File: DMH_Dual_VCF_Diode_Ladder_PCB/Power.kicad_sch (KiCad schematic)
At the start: 32 parts, among them J0 Conn_01x01, J100 IDC_02x08, U1 TL074, U2 TL074, U3 TL074, U4 TL074, U5 TL074, U6 TL074, U7 TL074

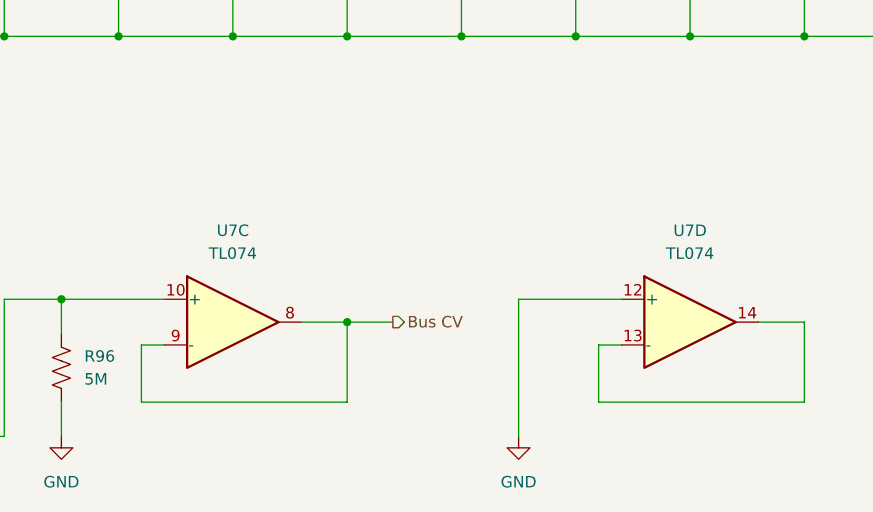
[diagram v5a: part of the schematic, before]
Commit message: Re-annotated OpAmps as per PCB layout
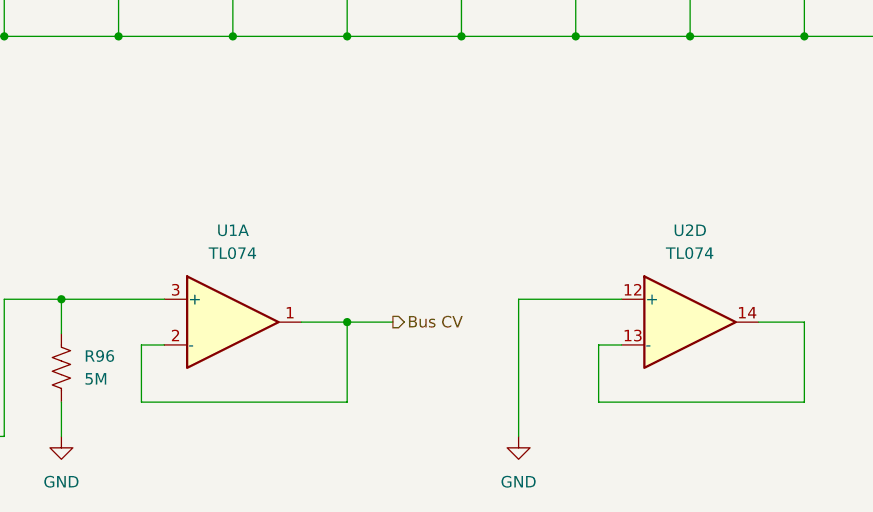
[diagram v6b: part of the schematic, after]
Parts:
- renumbered U7 to U1, U7 to U2
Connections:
- net Bus CV: now also U1.1, U1.2 (-); no longer U1.8, U1.9 (-)
- net at J100.7a (Pin_7a), J100.7b (Pin_7b), R96.1: now also U1.3 (+); no longer U1.10 (+)
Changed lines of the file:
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@@
+			)
+		)
+		(property "Function" ""
+			(at 167.64 120.65 0)
+			(effects
+				(font
+					(size 1.27 1.27)
+				)
 			)
 		)
@@
 		(dnp no)
 		(fields_autoplaced yes)
-		(property "Reference" "U7"
+		(property "Reference" "U2"
 			(at 152.4 167.64 0)
 			(effects
@@
 			)
 		)
+		(property "Function" ""
+			(at 152.4 177.8 0)
+			(effects
+				(font
+					(size 1.27 1.27)
+				)
+			)
+		)
 		(pin "10"
 		)
@@
 			(project ""
 				(path "/58f4306d-5387-4983-bb08-41a2313fd315/0cdf34b2-39cd-4d9e-981a-97cd34791509"
-					(reference "U7")
+					(reference "U2")
 					(unit 4)
 				)
@@
 			)
 		)
+		(property "Function" ""
+			(at 142.24 120.65 0)
+			(effects
+				(font
+					(size 1.27 1.27)
+				)
+			)
+		)
 		(pin "7"
 		)
@@
 			)
 		)
+		(property "Function" ""
+			(at 218.44 120.65 0)
+			(effects
+				(font
+					(size 1.27 1.27)
+				)
+			)
+		)
 		(pin "3"
 		)
@@
 				)
 				(hide yes)
+			)
+		)
+		(property "Function" ""
+			(at 116.84 120.65 0)
+			(effects
+				(font
+					(size 1.27 1.27)
+				)
 			)
 		)
@@
 		(lib_id "Amplifier_Operational:TL074")
 		(at 101.6 177.8 0)
-		(unit 3)
-		(exclude_from_sim no)
-		(in_bom yes)
-		(on_board yes)
-		(dnp no)
-		(property "Reference" "U7"
+		(unit 1)
+		(exclude_from_sim no)
+		(in_bom yes)
+		(on_board yes)
+		(dnp no)
+		(property "Reference" "U1"
 			(at 101.6 167.64 0)
 			(effects
@@
 			(project ""
 				(path "/58f4306d-5387-4983-bb08-41a2313fd315/0cdf34b2-39cd-4d9e-981a-97cd34791509"
-					(reference "U7")
-					(unit 3)
+					(reference "U1")
+					(unit 1)
 				)
 			)
@@
 			)
 		)
+		(property "Function" ""
+			(at 193.04 120.65 0)
+			(effects
+				(font
+					(size 1.27 1.27)
+				)
+			)
+		)
